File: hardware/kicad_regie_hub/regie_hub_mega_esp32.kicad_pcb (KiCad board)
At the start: 2 copper layers, 180 x 140 mm, 11 parts

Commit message: hardware: pistes routees sur les 3 cartes (Freerouting + kicad-cli pcb drc)
Autoroutage headless via Freerouting (pcbnew.ExportSpecctraDSN -> java -jar
freerouting.jar -> pcbnew.ImportSpecctraSES), pas un routage devine a la
main. Resultat verifie avec kicad-cli pcb drc reel sur les 3 cartes: 0
violation de clearance, 0 element non connecte. Seuls avertissements
restants: lib_footprint_mismatch (cosmetique) et quelques track_dangling
(residu mineur d'autorouter, a nettoyer dans KiCad, sans impact electrique).

Co-Authored-By: Claude Sonnet 5 <noreply@anthropic.com>
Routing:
- net GND: track 0.00 -> 266.7 mm
- net VCC_5V_MEGA: track 0.00 -> 155.3 mm
- net ESP32_RX2_3V3: track 0.00 -> 112.1 mm, vias 0 -> 1
- net NRF_VCC_DEDIE: track 0.00 -> 109.0 mm
- net MEGA_RX2_DIRECT: track 0.00 -> 77.0 mm
- net MEGA_RX3_DIRECT: track 0.00 -> 76.1 mm
- net MEGA_TX3_5V: track 0.00 -> 51.9 mm
- net NRF_MOSI: track 0.00 -> 51.7 mm
- net ESP32_RX1_3V3: track 0.00 -> 51.6 mm
- net NRF_SCK: track 0.00 -> 47.1 mm
- net NRF_CSN: track 0.00 -> 47.1 mm
- net NRF_CE: track 0.00 -> 47.1 mm
- net NRF_MISO: track 0.00 -> 46.1 mm
- net MEGA_TX2_5V: track 0.00 -> 35.0 mm

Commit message: hardware: nettoyage track_dangling + C3 rapproche de J_NRF sur le hub
Nano: 2 troncons de piste dupliques/morts (net NRF_SCK) identifies et
supprimes via script pcbnew, ne menaient a aucune pastille -- DRC propre
(0 track_dangling, 0 non connecte, seul lib_footprint_mismatch cosmetique
reste).

Hub: le nRF24 (J_NRF) et son condensateur de decouplage dedie (C3) etaient
a 25mm -- trop loin pour un decouplage propre a 2,4GHz. C3 repositionne a
12mm de J_NRF, carte entierement re-routee (Freerouting), puis 2 nouveaux
track_dangling (net VCC_5V_MEGA) nettoyes de la meme facon. DRC final: 0
violation de clearance, 0 non connecte, 0 track_dangling.

Co-Authored-By: Claude Sonnet 5 <noreply@anthropic.com>
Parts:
- moved C3 13.0 mm to (152.0, 20.0)
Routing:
- net ESP32_RX2_3V3: track 112.1 -> 59.9 mm, vias 1 -> 0
- net NRF_VCC_DEDIE: track 109.0 -> 95.5 mm
- net GND: track 266.7 -> 253.7 mm
- net VCC_5V_MEGA: track 155.3 -> 155.0 mm, vias 0 -> 1

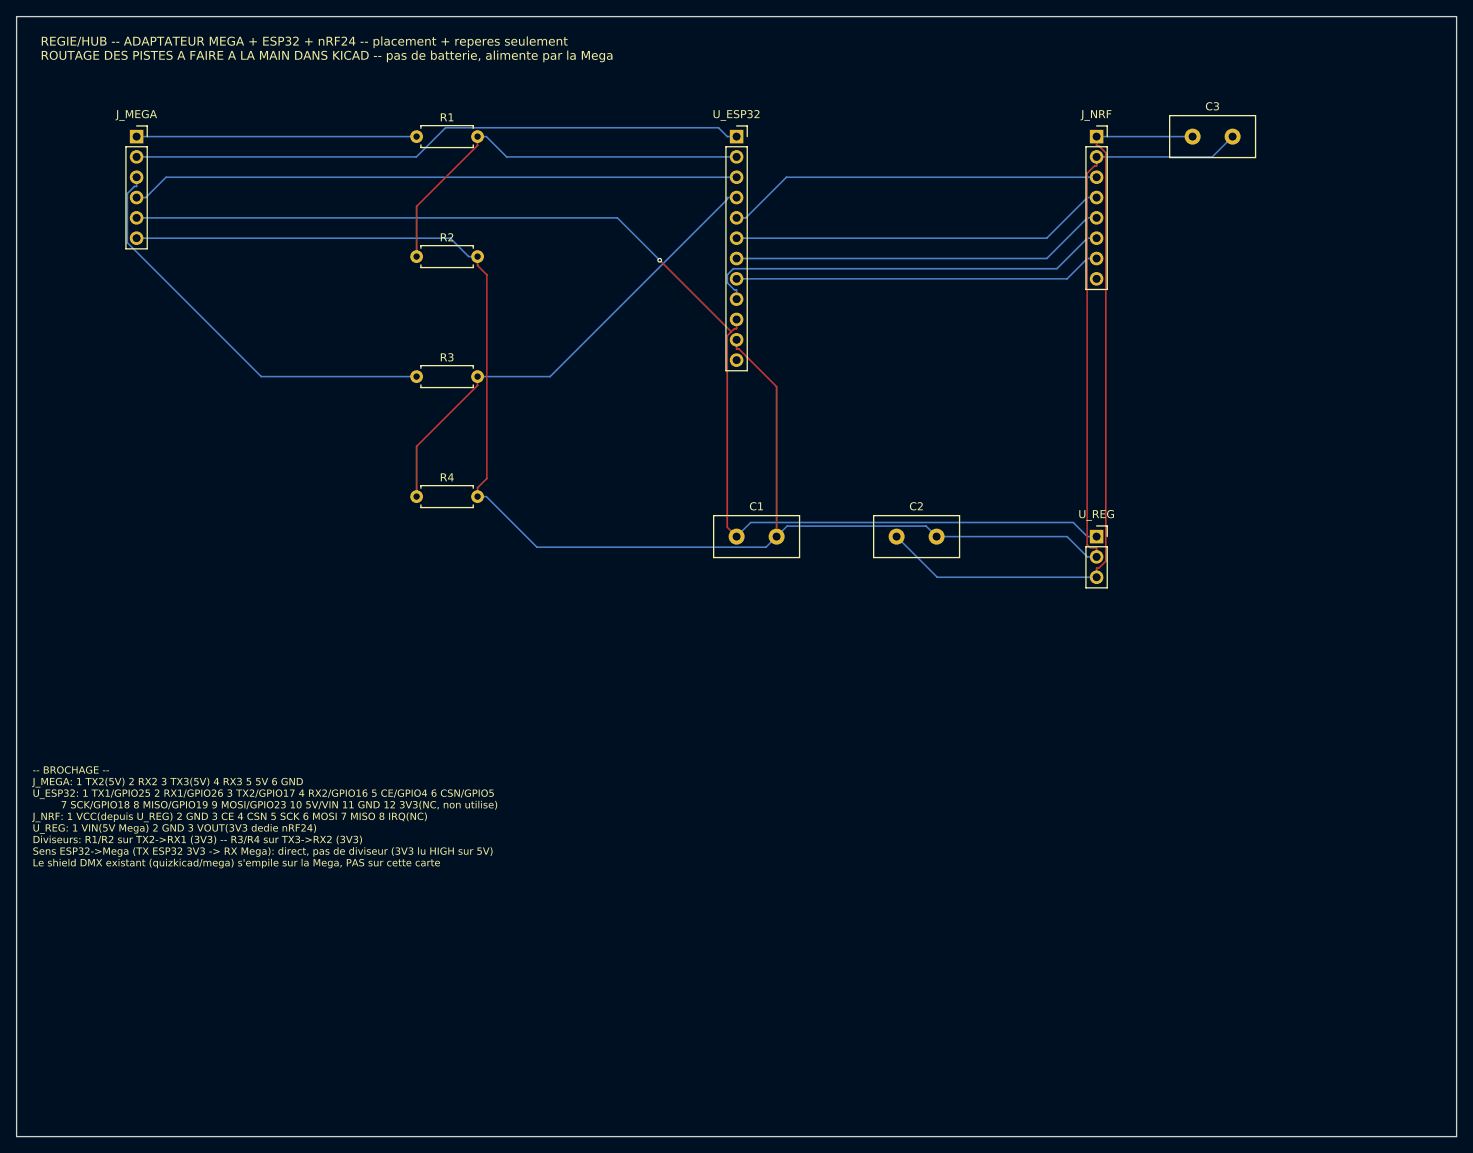
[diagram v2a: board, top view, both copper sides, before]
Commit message: hardware: vrais ports femelles pour les modules (Nano, ESP32 x2) + reroutage
Remplace les empreintes abstraites/simplifiees par de vraies barrettes
femelles PinSocket, dimensionnees et brochees pour correspondre aux modules
physiques reels, sur les 3 cartes:

- Nano (buzzer equipe): 2x PinSocket_1x15 (A1L/A1R, 30 broches, entraxe
  15,24mm) au lieu de l'empreinte "Nano soude directement" -- numerotation
  verifiee contre la vraie empreinte Module:Arduino_Nano.
- ESP32 buzzer (secours): 2x PinSocket_1x19 (U1L/U1R, 38 broches, entraxe
  22,86mm) au lieu du connecteur 4 broches abstrait -- brochage GPIO4/
  GPIO13/VIN/GND positionne selon le layout generique 38 broches le plus
  courant (verifie en ligne), avec avertissement clair dans le README:
  plusieurs variantes de clones existent, a verifier sur le module recu.
- ESP32 hub (regie): 2x PinSocket_1x15 (U_ESP32L/R, 30 broches, entraxe
  15,24mm) au lieu du connecteur 12 broches abstrait -- brochage DOIT ESP32
  DevKit V1 verifie (le modele exact confirme par le client), design de
  reference unique donc plus fiable que les clones 38 broches.

Les 34/19 broches physiques non utilisees sur chaque module restent
presentes sans net (fixation mecanique uniquement). Toutes les cartes
re-routees (Freerouting) et revalidees (kicad-cli pcb drc): 0 violation de
clearance, 0 element non connecte, 0 track_dangling restant (nettoyage
verifie topologie par topologie pour ne pas casser une piste utile).

Co-Authored-By: Claude Sonnet 5 <noreply@anthropic.com>
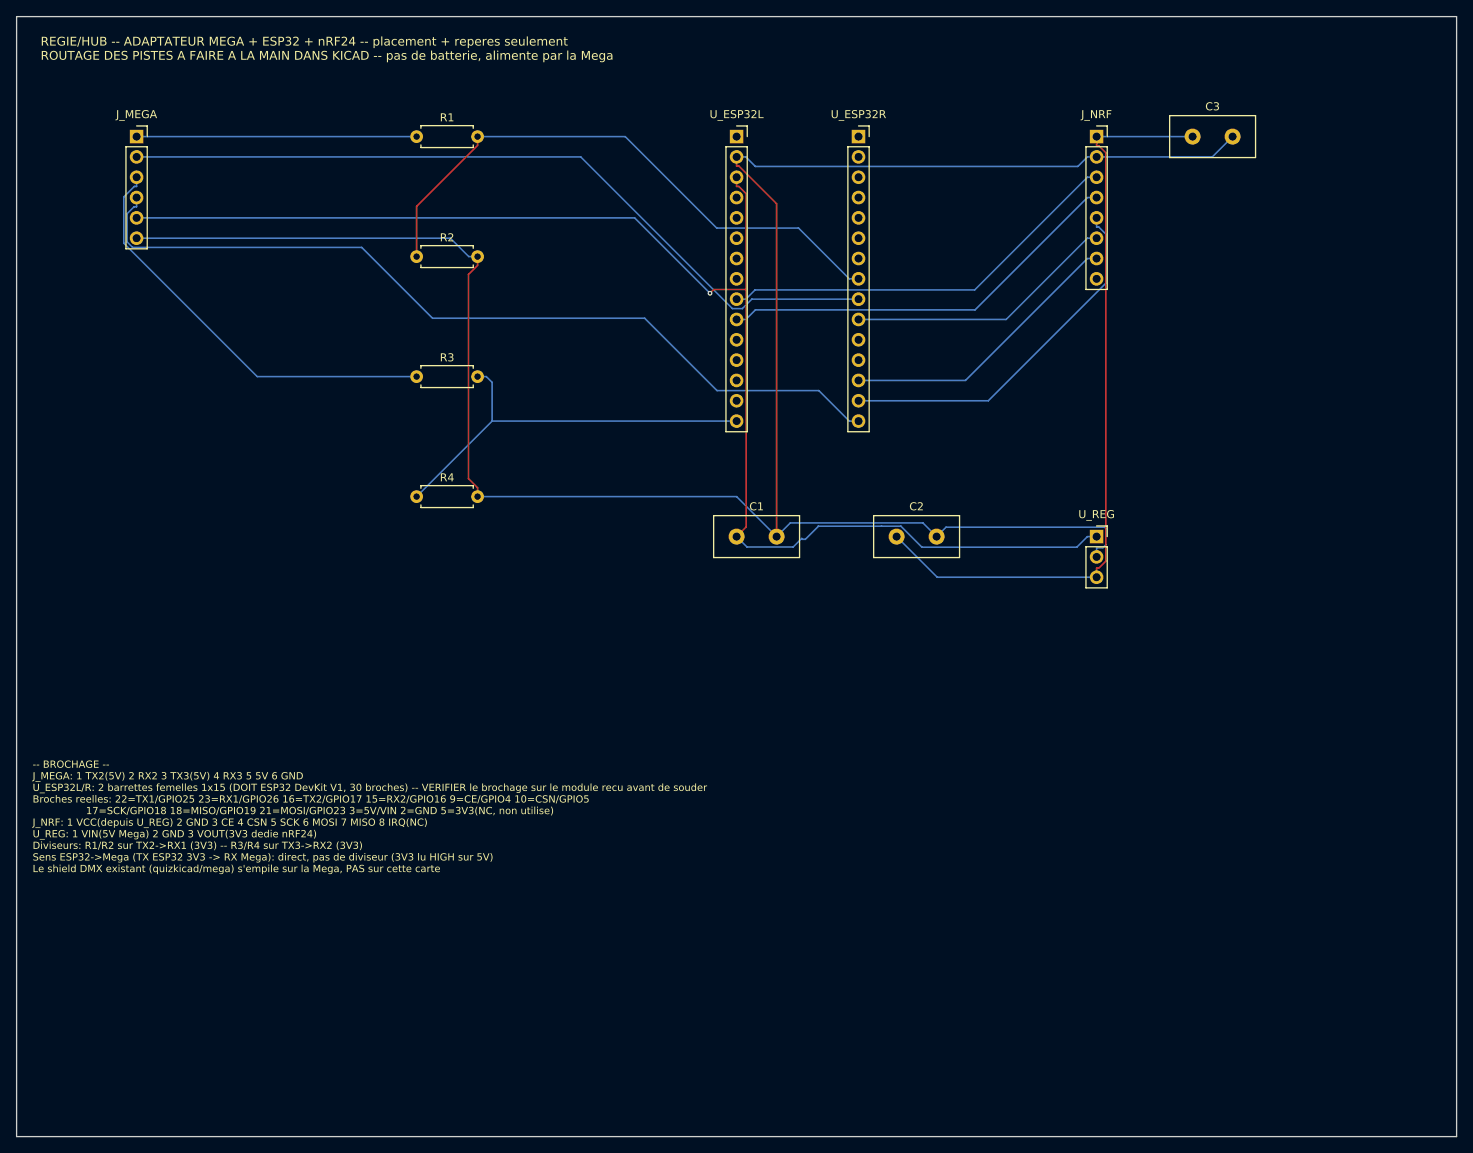
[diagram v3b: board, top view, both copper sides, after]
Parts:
- removed U_ESP32: Vers ESP32 DevKit V1 (FT232, headers femelles), Connector_PinSocket_2.54mm:PinSocket_1x12_P2.54mm_Vertical
- added U_ESP32L: ESP32 DevKit V1 colonne gauche (broches 1-15), Connector_PinSocket_2.54mm:PinSocket_1x15_P2.54mm_Vertical, F.Cu at (95.0, 20.0)
- added U_ESP32R: ESP32 DevKit V1 colonne droite (broches 16-30), Connector_PinSocket_2.54mm:PinSocket_1x15_P2.54mm_Vertical, F.Cu at (110.2, 20.0)
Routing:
- net MEGA_RX3_DIRECT: track 76.1 -> 106.9 mm
- net MEGA_RX2_DIRECT: track 77.0 -> 98.6 mm
- net GND: track 253.7 -> 275.3 mm
- net ESP32_RX1_3V3: track 51.6 -> 73.1 mm
- net VCC_5V_MEGA: track 155.0 -> 174.7 mm
- net NRF_MOSI: track 51.7 -> 34.0 mm
- net NRF_MISO: track 46.1 -> 36.1 mm
- net ESP32_RX2_3V3: track 59.9 -> 50.9 mm
- net NRF_CE: track 47.1 -> 51.3 mm
- net NRF_CSN: track 47.1 -> 51.3 mm
- net NRF_SCK: track 47.1 -> 45.8 mm
- net MEGA_TX3_5V: track 51.9 -> 52.6 mm
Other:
- board text added: "-- BROCHAGE -- J_MEGA: 1 TX2(5V) 2 RX2 3 TX3(5V) 4 RX3 5 5V 6 GND U_ESP32L/R: 2 barrettes femelles 1x15 (DOIT ESP32 DevKit V1, 30 broches) -- VERIFIER le brochage sur le module recu avant de souder Broches reelles: 22=TX1/GPIO25 23=RX1/GPIO26 16=TX2/GPIO17 15=RX2/GPIO16 9=CE/GPIO4 10=CSN/GPIO5 17=SCK/GPIO18 18=MISO/GPIO19 21=MOSI/GPIO23 3=5V/VIN 2=GND 5=3V3(NC, non utilise) J_NRF: 1 VCC(depuis U_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"
- board text removed: "-- BROCHAGE -- J_MEGA: 1 TX2(5V) 2 RX2 3 TX3(5V) 4 RX3 5 5V 6 GND U_ESP32: 1 TX1/GPIO25 2 RX1/GPIO26 3 TX2/GPIO17 4 RX2/GPIO16 5 CE/GPIO4 6 CSN/GPIO5 7 SCK/GPIO18 8 MISO/GPIO19 9 MOSI/GPIO23 10 5V/VIN 11 GND 12 3V3(NC, non utilise) J_NRF: 1 VCC(depuis U_REG) 2 GND 3 CE 4 CSN 5 SCK 6 MOSI 7 MISO 8 IRQ(NC) U_REG: 1 VIN(5V Mega) 2 GND 3 VOUT(3V3 dedie nRF24) Diviseurs: R1/R2 sur TX2->RX1 (3V3) -- R3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"

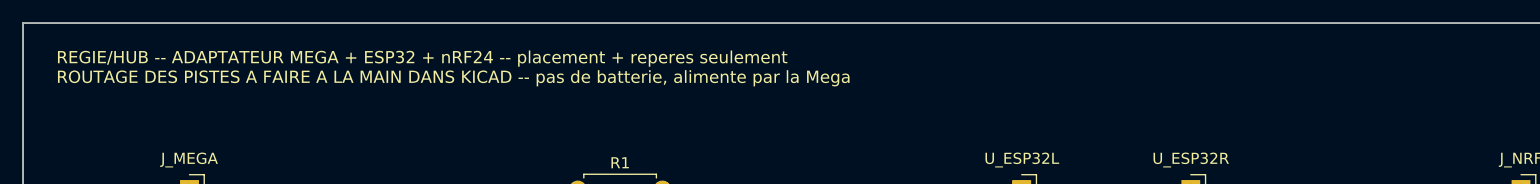
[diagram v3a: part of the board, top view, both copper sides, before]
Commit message: hardware: retire la mention "routage a faire a la main" (obsolete)
Le texte de titre sur la serigraphie des 3 cartes disait encore "ROUTAGE
DES PISTES A FAIRE A LA MAIN DANS KICAD", ecrit avant que le routage ne
soit fait via Freerouting. Remplace par une mention correcte ("pistes
routees (Freerouting), a relire avant fabrication"). Edition de texte
seule sur les fichiers deja routes -- aucune piste/pastille touchee,
DRC revalide identique (0 violation de clearance, 0 non connecte).

Co-Authored-By: Claude Sonnet 5 <noreply@anthropic.com>
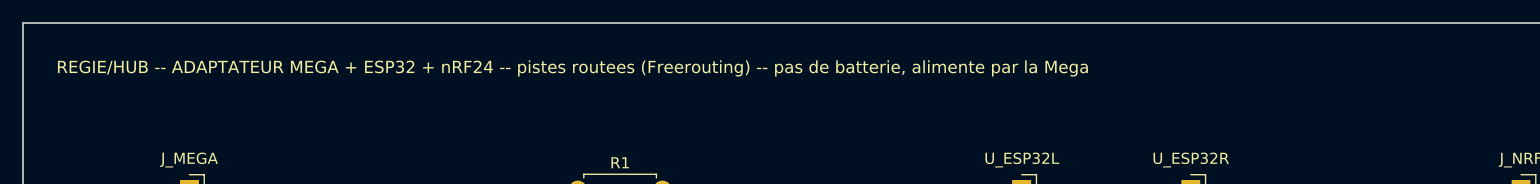
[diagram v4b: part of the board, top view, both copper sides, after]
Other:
- board text added: "REGIE/HUB -- ADAPTATEUR MEGA + ESP32 + nRF24 -- pistes routees (Freerouting) -- pas de batterie, alimente par la Mega"
- board text removed: "REGIE/HUB -- ADAPTATEUR MEGA + ESP32 + nRF24 -- placement + reperes seulement ROUTAGE DES PISTES A FAIRE A LA MAIN DANS KICAD -- pas de batterie, alimente par la Mega"
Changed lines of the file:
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@@
 		)
 	)
-	(gr_text "REGIE/HUB -- ADAPTATEUR MEGA + ESP32 + nRF24 -- placement + reperes seulement\nROUTAGE DES PISTES A FAIRE A LA MAIN DANS KICAD -- pas de batterie, alimente par la Mega"
+	(gr_text "REGIE/HUB -- ADAPTATEUR MEGA + ESP32 + nRF24 -- pistes routees (Freerouting) -- pas de batterie, alimente par la Mega"
 		(at 8 9 0)
 		(layer "F.SilkS")

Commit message: hardware: titres serigraphie simplifies (retire tout commentaire de process)
Le titre en haut de chaque carte disait encore des phrases du type "pistes
routees (Freerouting), a relire avant fabrication" -- du commentaire sur le
processus de generation, pas quelque chose qui a sa place gravee sur un vrai
circuit fabrique. Remplace par un simple nom de carte ("BUZZER EQUIPE -
NANO", "BUZZER EQUIPE - ESP32", "REGIE HUB"). Le bloc BROCHAGE (guide de
soudage demande explicitement) reste inchange. Edition de texte seule,
DRC revalide identique sur les 3 cartes.

Co-Authored-By: Claude Sonnet 5 <noreply@anthropic.com>
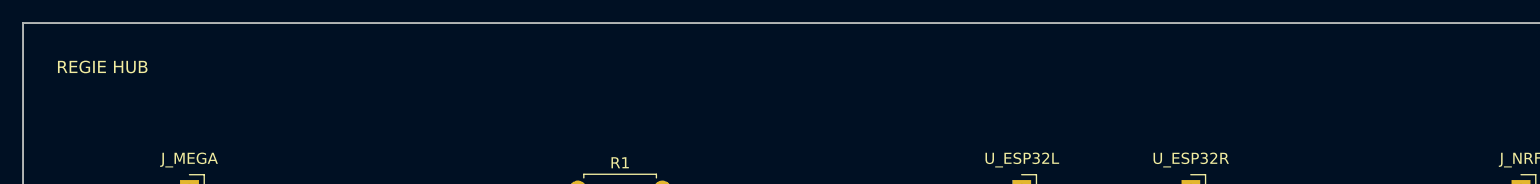
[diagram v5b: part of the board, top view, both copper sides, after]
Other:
- board text added: "REGIE HUB"
- board text removed: "REGIE/HUB -- ADAPTATEUR MEGA + ESP32 + nRF24 -- pistes routees (Freerouting) -- pas de batterie, alimente par la Mega"
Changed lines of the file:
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@@
 		)
 	)
-	(gr_text "REGIE/HUB -- ADAPTATEUR MEGA + ESP32 + nRF24 -- pistes routees (Freerouting) -- pas de batterie, alimente par la Mega"
+	(gr_text "REGIE HUB"
 		(at 8 9 0)
 		(layer "F.SilkS")
